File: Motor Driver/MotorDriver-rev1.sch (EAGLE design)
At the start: 9 parts, among them CN1 3p-2.54, Q1 CJ2302

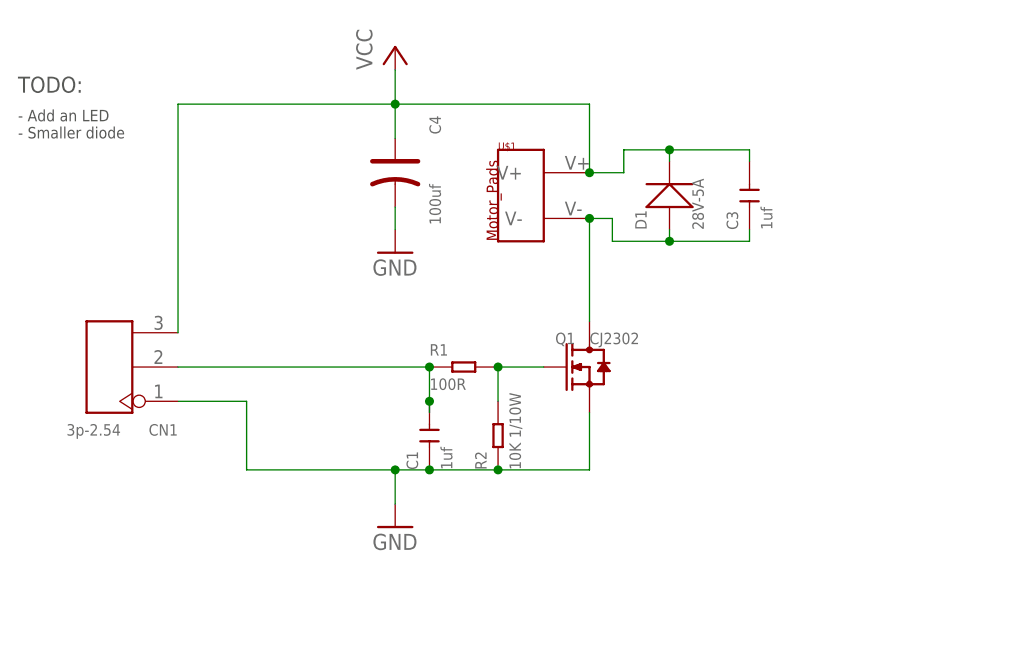
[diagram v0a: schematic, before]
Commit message: New remote, new motor driver
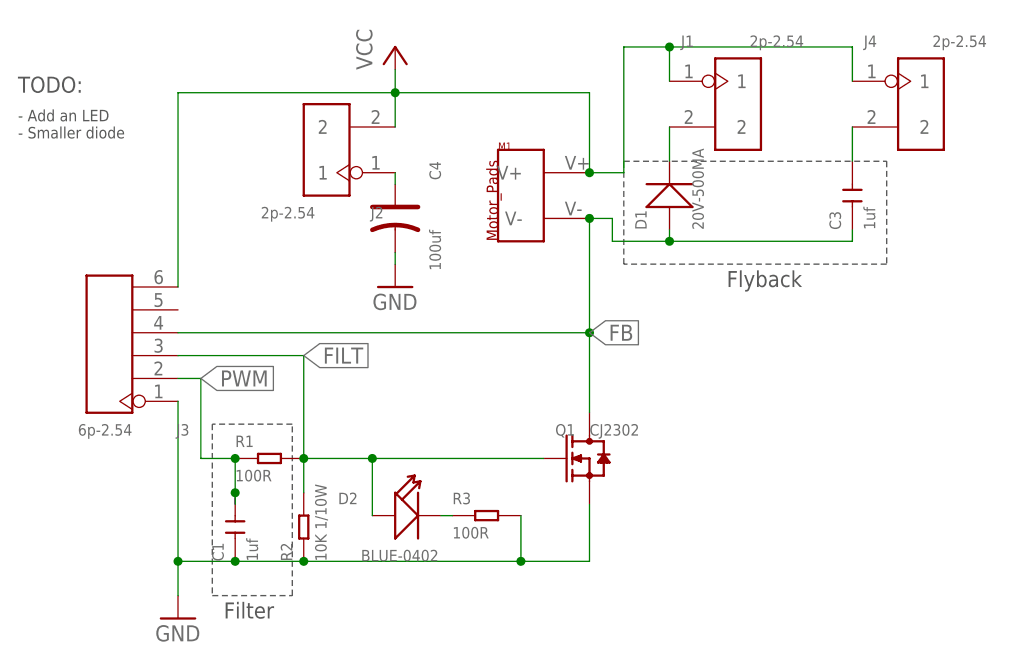
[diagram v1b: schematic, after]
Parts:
- removed CN1: 3p-2.54, Seeed-Connector -2016:DIP-BLACK-MALE-HEADER-VERT(3P-2.54)
- added D2: BLUE-0402, Seeed-LED-2016:SMD-LED-CLEAR-BLUE(0402)
- added J1, J2, J4: 2p-2.54, Seeed-Connector -2016:DIP-BLACK-MALE-HEADER-VERT(2P-2.54)
- added J3: 6p-2.54, Seeed-Connector -2016:DIP-BLACK-MALE-HEADER(6P-2.54)
- added R3: 100R, Seeed-Resistor-2016:SMD-RES-100R-5%-1/16W(0402)
- D1: value 28V-5A -> 20V-500MA; device Seeed-Diode-2016:SMD-DIODE-SCHOTTKY-28V-5A(DO-214AA) -> Seeed-Diode-2016:SMD-DIODE-SCHOTTKY-20V-500MA(SOD-123)
- renumbered U$1 to M1
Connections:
- removed net N$3: C1.2, CN1.P$2, R1.1
- removed net N$4: Q1.G, R1.2, R2.2
- removed net N$6: C3.1, D1.+, M1.V-, Q1.D
- new net FB: C3.1, D1.+, J3.4, M1.V-, Q1.D
- new net FILT: D2.+, J3.3, Q1.G, R1.2, R2.2
- new net N$1: D2.-, R3.1
- new net N$5: C4.+, J2.1
- new net N$7: D1.-, J1.2
- new net N$8: C3.2, J4.2
- new net PWM: C1.2, J3.2, R1.1
- net GND: now also J3.1, R3.2; no longer CN1.P$1
- net VCC: now also J1.1, J2.2, J3.6, J4.1; no longer C3.2, C4.+, CN1.P$3, D1.-
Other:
- note added: "Filter"
- note added: "Flyback"
- moved on the sheet: C1, C3, C4, Q1, R1, R2
